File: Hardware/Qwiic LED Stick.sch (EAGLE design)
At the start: 39 parts, among them J2 SMD, J3 PTH, J4 SMD, J6 AVR_SPI_PROG_3X2TESTPOINTS, U1 Tiny85-20-SMT

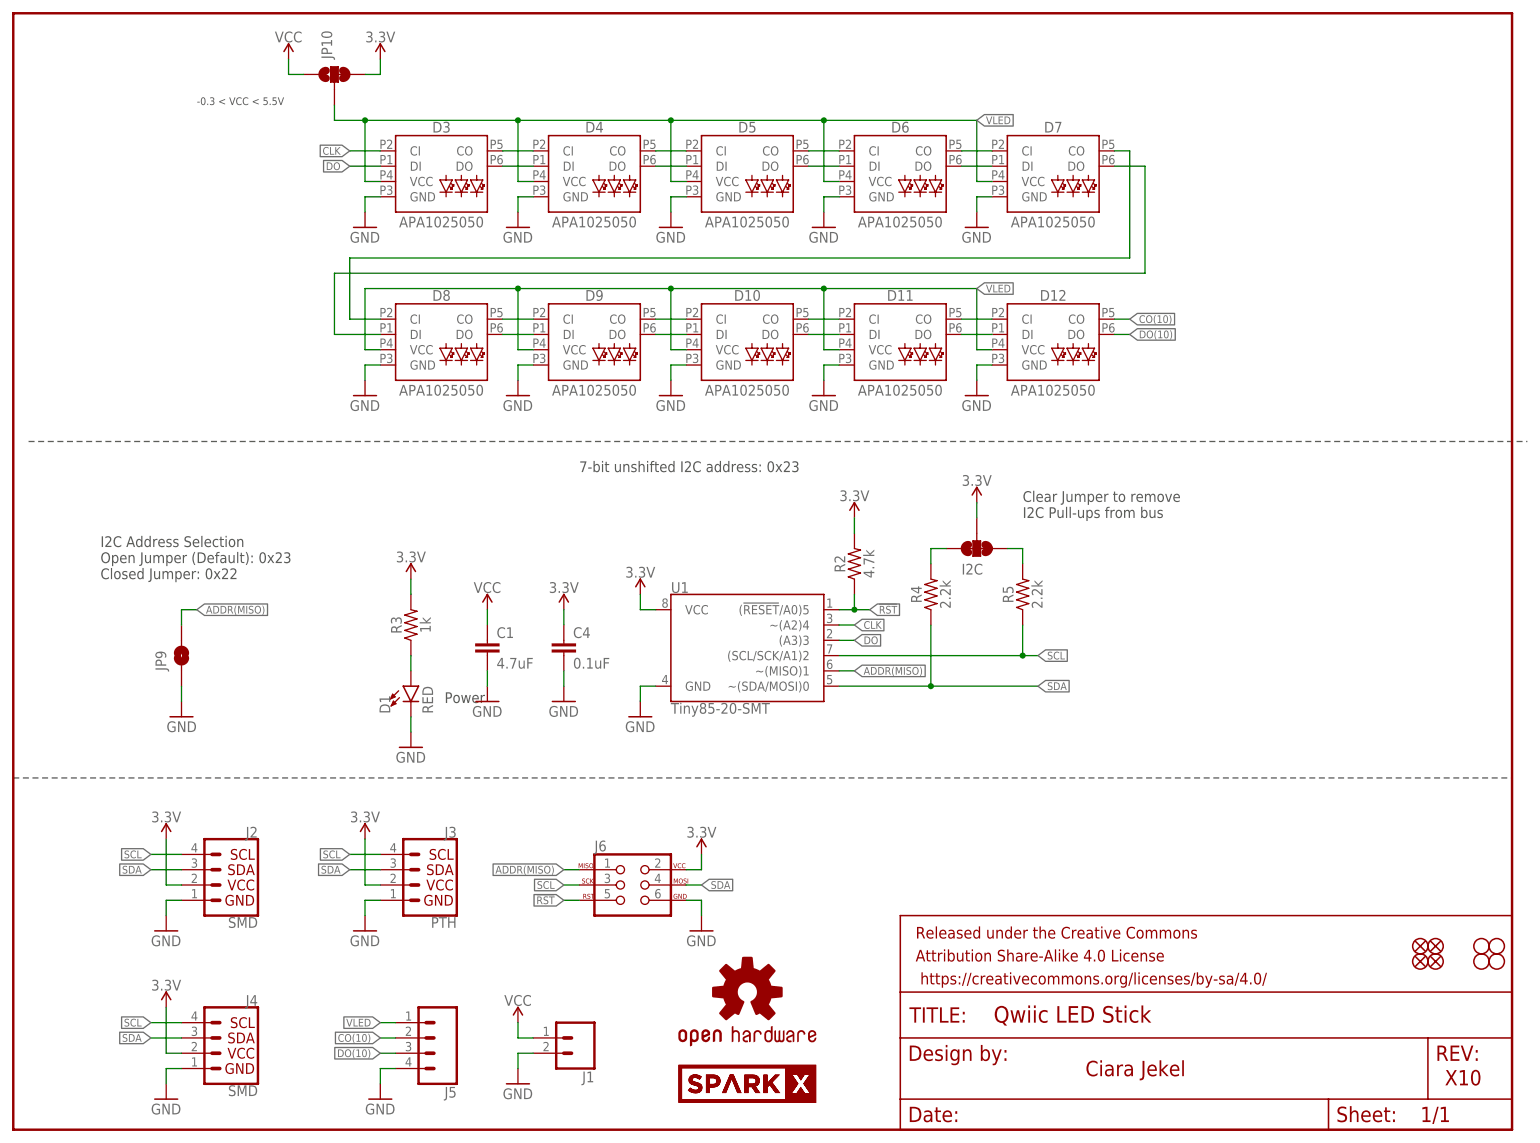
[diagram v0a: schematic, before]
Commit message: update schematic
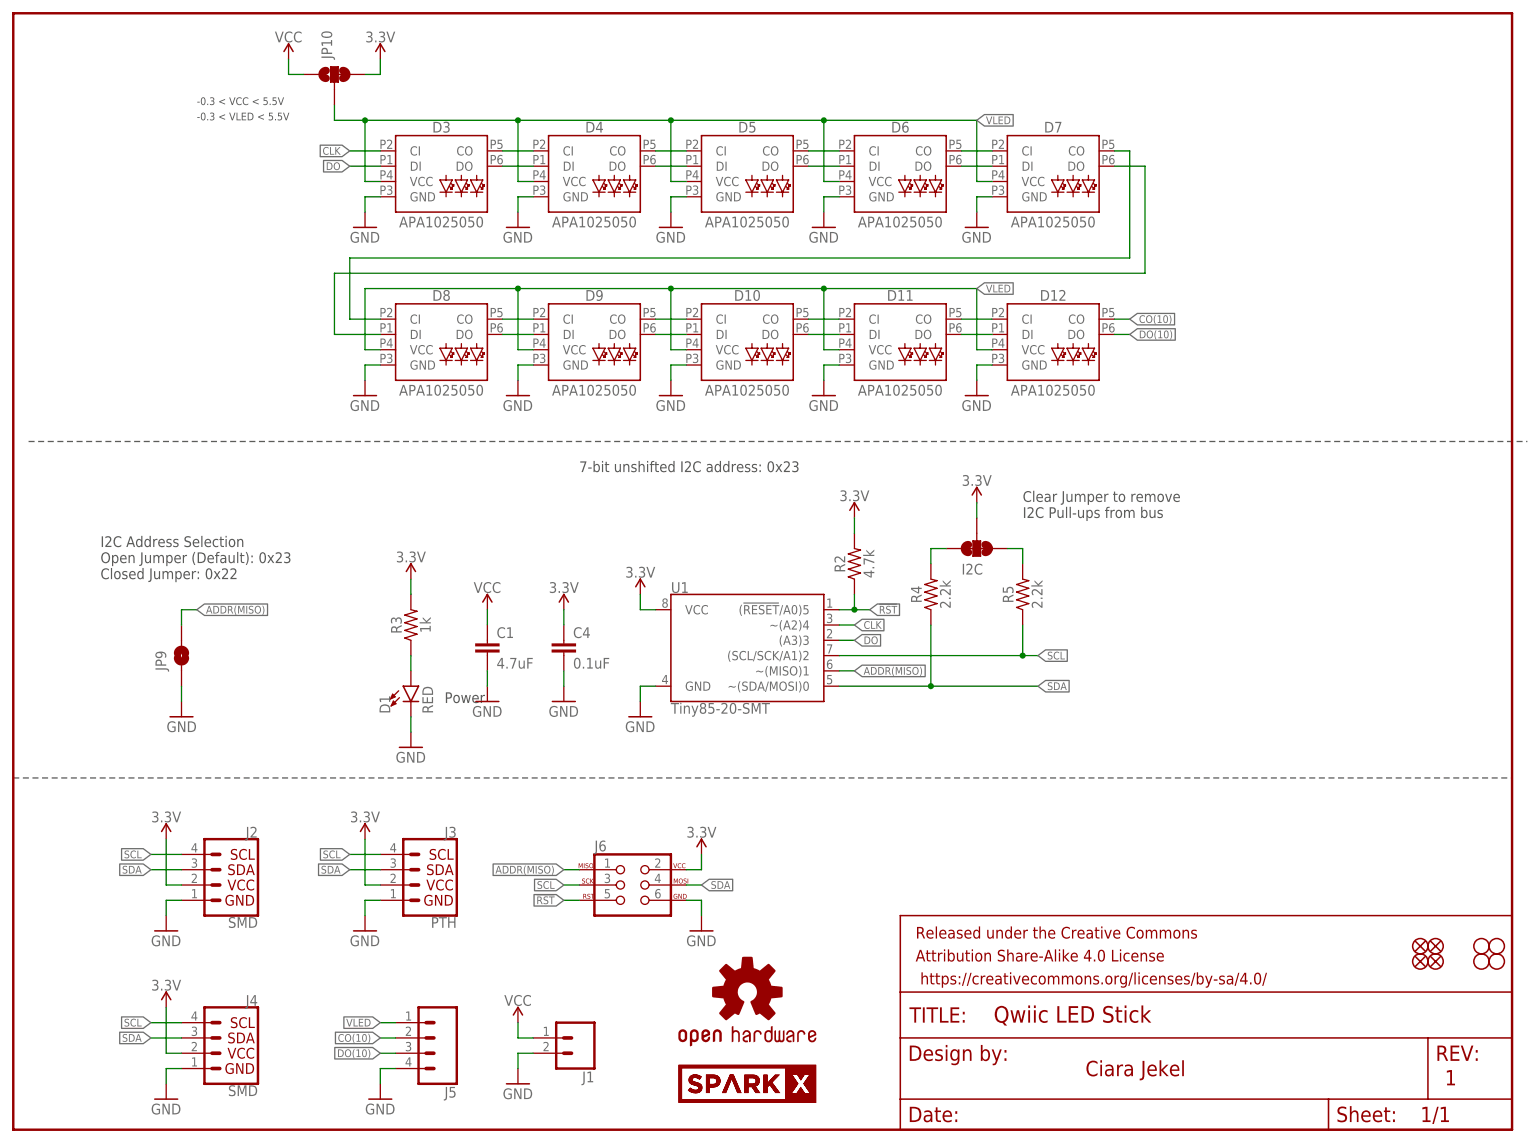
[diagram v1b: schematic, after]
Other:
- note added: "-0.3 < VLED < 5.5V"
- note added: "1"
- note removed: "X10"
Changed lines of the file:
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@@
 <sheet>
 <plain>
-<text x="237.744" y="7.366" size="2.54" layer="94">X10</text>
+<text x="237.744" y="7.366" size="2.54" layer="94">1</text>
 <text x="167.64" y="101.6" size="1.778" layer="97">Clear Jumper to remove
 I2C Pull-ups from bus</text>
@@
 <wire x1="2.54" y1="114.3" x2="251.46" y2="114.3" width="0.2032" layer="97" style="longdash"/>
 <text x="30.48" y="170.18" size="1.27" layer="97">-0.3 &lt; VCC &lt; 5.5V</text>
+<text x="30.48" y="167.64" size="1.27" layer="97">-0.3 &lt; VLED &lt; 5.5V</text>
 </plain>
 <instances>
